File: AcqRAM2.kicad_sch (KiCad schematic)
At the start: 206 parts, among them U30 MSM5416283, U31 MSM5416283, U32 MSM5416283, U33 MSM5416283, U39 MSM5416283, U40 MSM5416283, U41 MSM5416283, U42 MSM5416283, U43 MSM5416283, U50 MSM5416283, U51 MSM5416283, U52 MSM5416283, U53 MSM5416283, U58 MSM5416283, U59 MSM5416283, U60 MSM5416283, U61 MSM5416283

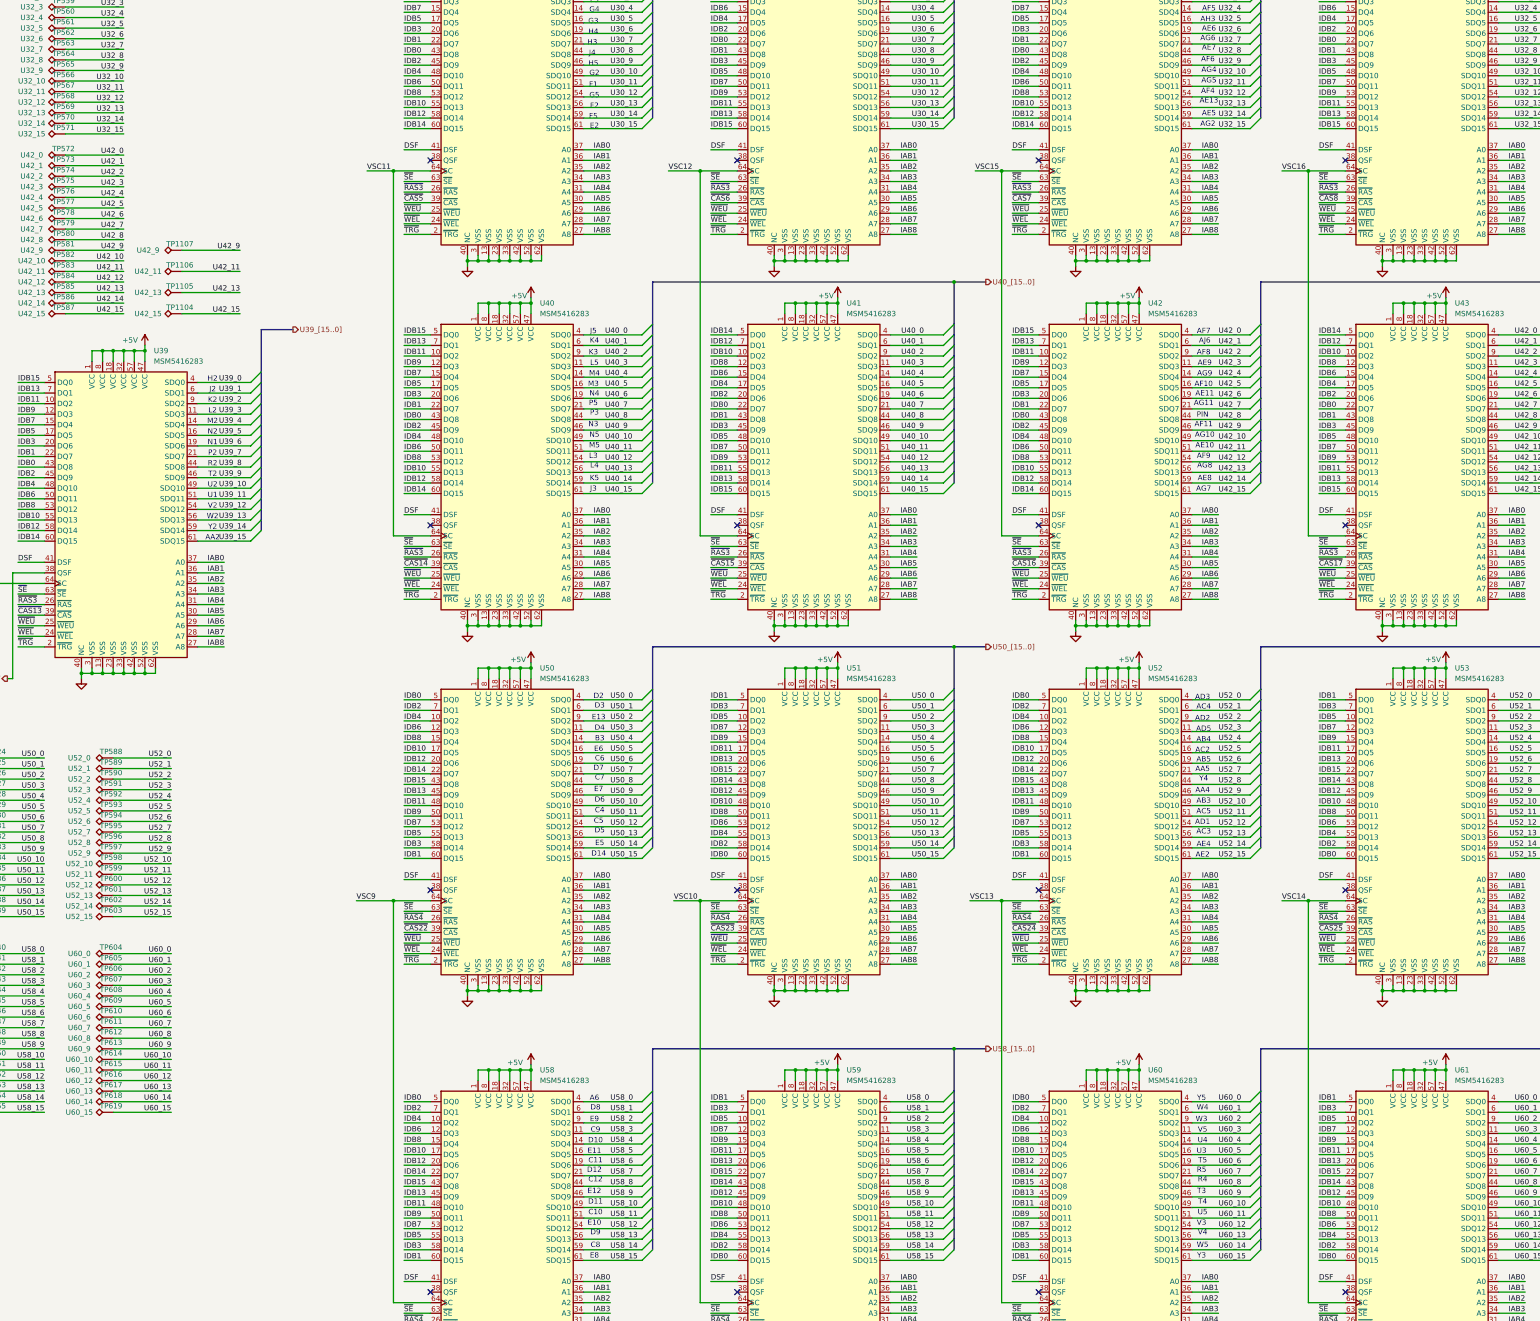
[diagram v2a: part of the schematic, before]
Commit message: Add pv names to VRAM chips
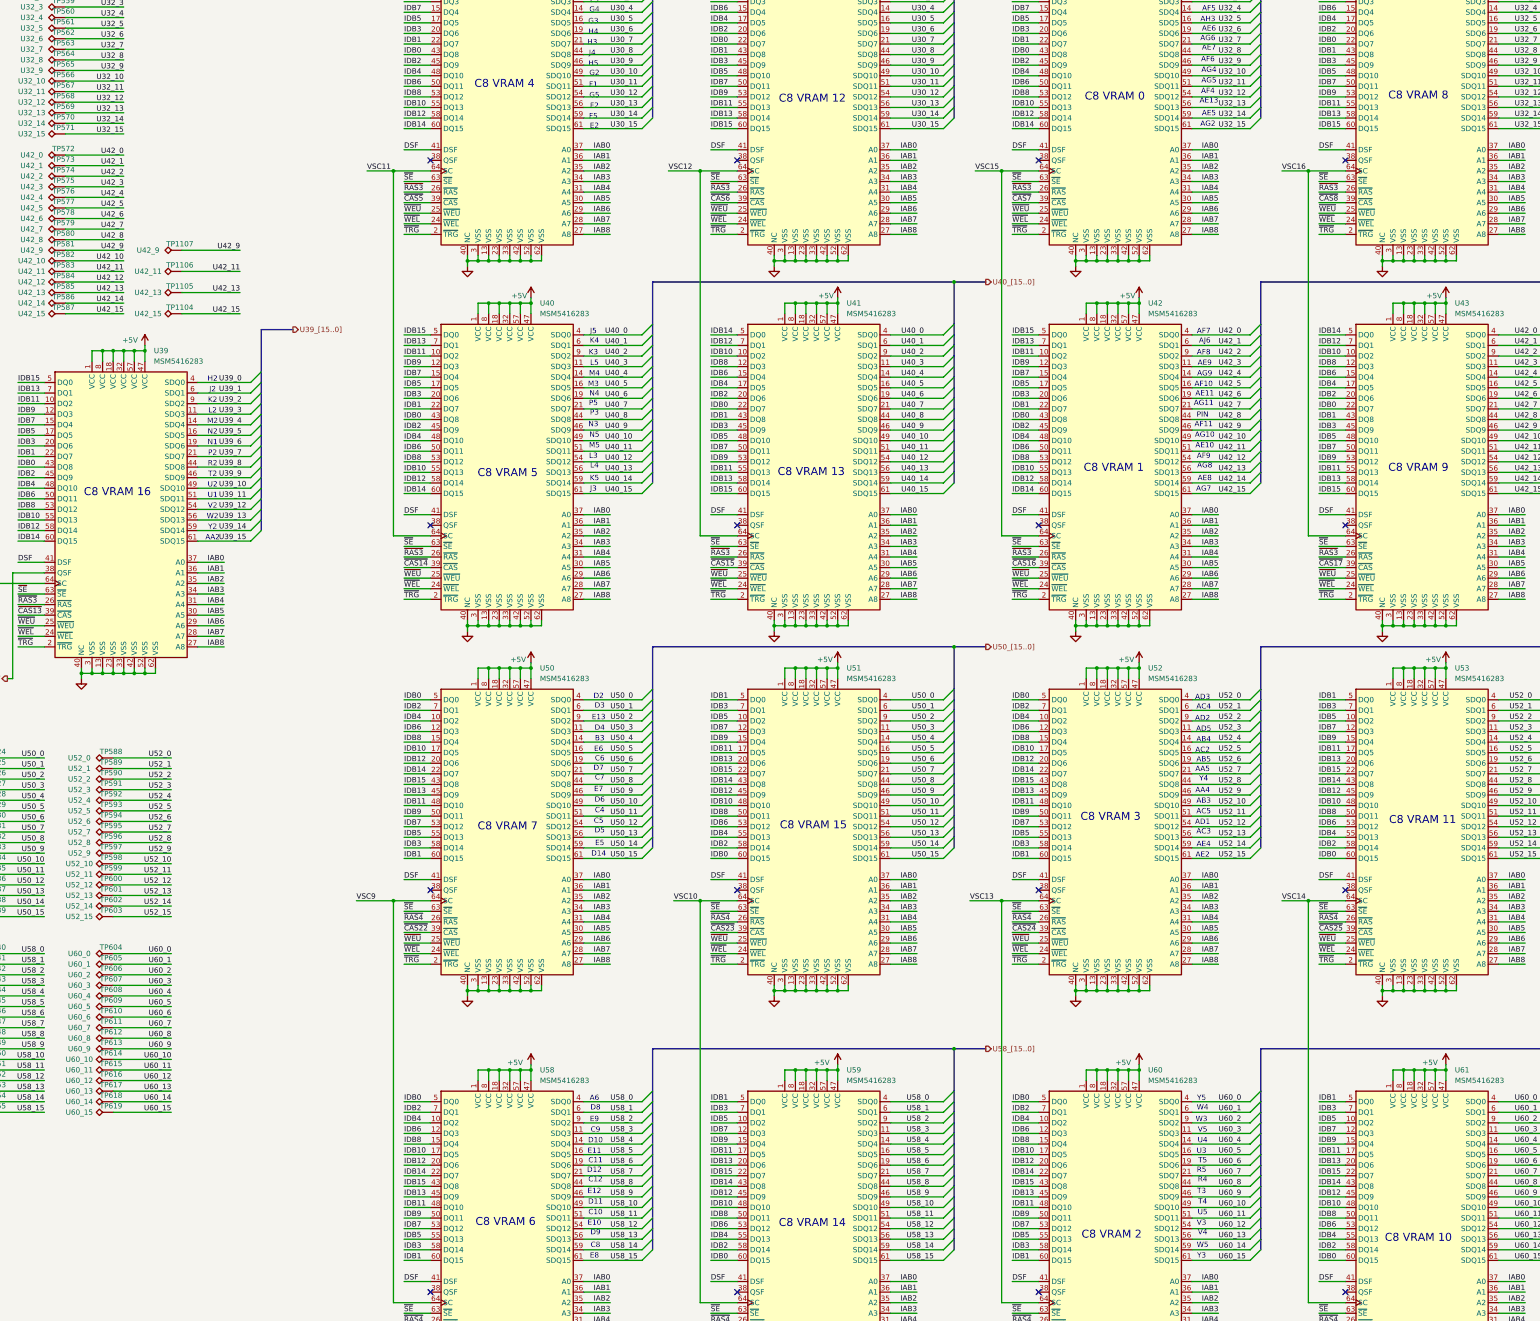
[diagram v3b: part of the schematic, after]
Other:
- note added: "C8 VRAM 0"
- note added: "C8 VRAM 1"
- note added: "C8 VRAM 10"
- note added: "C8 VRAM 11"
- note added: "C8 VRAM 12"
- note added: "C8 VRAM 13"
- note added: "C8 VRAM 14"
- note added: "C8 VRAM 15"
- note added: "C8 VRAM 16"
- note added: "C8 VRAM 2"
- note added: "C8 VRAM 3"
- note added: "C8 VRAM 4"
- note added: "C8 VRAM 5"
- note added: "C8 VRAM 6"
- note added: "C8 VRAM 7"
- note added: "C8 VRAM 8"
- note added: "C8 VRAM 9"
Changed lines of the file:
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@@
+		)
+	)
+	(text "C8 VRAM 11"
+		(exclude_from_sim no)
+		(at 457.962 230.886 0)
+		(effects
+			(font
+				(size 1.905 1.905)
+			)
 		)
 	)
@@
 		)
 	)
+	(text "C8 VRAM 10"
+		(exclude_from_sim no)
+		(at 456.946 331.216 0)
+		(effects
+			(font
+				(size 1.905 1.905)
+			)
+		)
+	)
 	(text "J2"
 		(exclude_from_sim no)
@@
 		)
 	)
+	(text "C8 VRAM 0"
+		(exclude_from_sim no)
+		(at 384.048 57.15 0)
+		(effects
+			(font
+				(size 1.905 1.905)
+			)
+		)
+	)
+	(text "C8 VRAM 2"
+		(exclude_from_sim no)
+		(at 383.286 330.454 0)
+		(effects
+			(font
+				(size 1.905 1.905)
+			)
+		)
+	)
 	(text "D10"
 		(exclude_from_sim no)
@@
 		)
 	)
+	(text "C8 VRAM 12"
+		(exclude_from_sim no)
+		(at 311.404 57.658 0)
+		(effects
+			(font
+				(size 1.905 1.905)
+			)
+		)
+	)
+	(text "C8 VRAM 6"
+		(exclude_from_sim no)
+		(at 237.744 327.406 0)
+		(effects
+			(font
+				(size 1.905 1.905)
+			)
+		)
+	)
 	(text "N4"
 		(exclude_from_sim no)
@@
 		)
 	)
+	(text "C8 VRAM 5"
+		(exclude_from_sim no)
+		(at 238.252 147.574 0)
+		(effects
+			(font
+				(size 1.905 1.905)
+			)
+		)
+	)
 	(text "R2"
 		(exclude_from_sim no)
@@
 		)
 	)
+	(text "C8 VRAM 15"
+		(exclude_from_sim no)
+		(at 311.658 232.156 0)
+		(effects
+			(font
+				(size 1.905 1.905)
+			)
+		)
+	)
 	(text "K2"
 		(exclude_from_sim no)
@@
 		)
 	)
+	(text "C8 VRAM 3"
+		(exclude_from_sim no)
+		(at 383.032 230.124 0)
+		(effects
+			(font
+				(size 1.905 1.905)
+			)
+		)
+	)
 	(text "C7"
 		(exclude_from_sim no)
@@
 		)
 	)
+	(text "C8 VRAM 1"
+		(exclude_from_sim no)
+		(at 383.794 146.304 0)
+		(effects
+			(font
+				(size 1.905 1.905)
+			)
+		)
+	)
 	(text "L2"
 		(exclude_from_sim no)
@@
 		)
 	)
+	(text "C8 VRAM 4"
+		(exclude_from_sim no)
+		(at 237.49 54.102 0)
+		(effects
+			(font
+				(size 1.905 1.905)
+			)
+		)
+	)
 	(text "W2"
 		(exclude_from_sim no)
@@
 		)
 	)
+	(text "C8 VRAM 8"
+		(exclude_from_sim no)
+		(at 456.946 56.896 0)
+		(effects
+			(font
+				(size 1.905 1.905)
+			)
+		)
+	)
 	(text "E5"
 		(exclude_from_sim no)
@@
 		)
 	)
+	(text "C8 VRAM 14"
+		(exclude_from_sim no)
+		(at 311.404 327.66 0)
+		(effects
+			(font
+				(size 1.905 1.905)
+			)
+		)
+	)
 	(text "C12"
 		(exclude_from_sim no)
@@
 		)
 	)
+	(text "C8 VRAM 13"
+		(exclude_from_sim no)
+		(at 311.15 147.32 0)
+		(effects
+			(font
+				(size 1.905 1.905)
+			)
+		)
+	)
+	(text "C8 VRAM 9"
+		(exclude_from_sim no)
+		(at 456.946 146.304 0)
+		(effects
+			(font
+				(size 1.905 1.905)
+			)
+		)
+	)
 	(text "AB5"
 		(exclude_from_sim no)
@@
 		)
 	)
+	(text "C8 VRAM 16"
+		(exclude_from_sim no)
+		(at 144.526 152.146 0)
+		(effects
+			(font
+				(size 1.905 1.905)
+			)
+		)
+	)
 	(text "R5"
 		(exclude_from_sim no)
@@
 			)
 		)
+	)
+	(text "C8 VRAM 7"
+		(exclude_from_sim no)
+		(at 238.252 232.41 0)
+		(effects
+			(font
+				(size 1.905 1.905)
+			)
+		)
